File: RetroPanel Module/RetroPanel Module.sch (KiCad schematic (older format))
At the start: 58 parts, among them J1 Front Panel, J10 SW_EXTRA, J16 SPEAKER, J17 LED_HDD, J2 SW_POWER, J3 LED_POWER, J4 SW_RESET, J5 SW_TURBO, J6 LED_TURBO, J7 POWER, J8 IIC, J9 POST_CARD, M1 Mounting_Pin, M10 Mounting_Pad, M11 Mounting_Pad, M12 Mounting_Pad, M13 Mounting_Pad, M14 Mounting_Pad, M15 Mounting_Pad, M16 Mounting_Pin, M2 Mounting_Pin, M3 Mounting_Pin, M4 Mounting_Pad, M5 Mounting_Pad, M6 Mounting_Pad, M7 Mounting_Pad, M8 Mounting_Pad, M9 Mounting_Pad, Q1 2N3904, Q2 2N3904, Q3 2N3904, Q4 2N3904

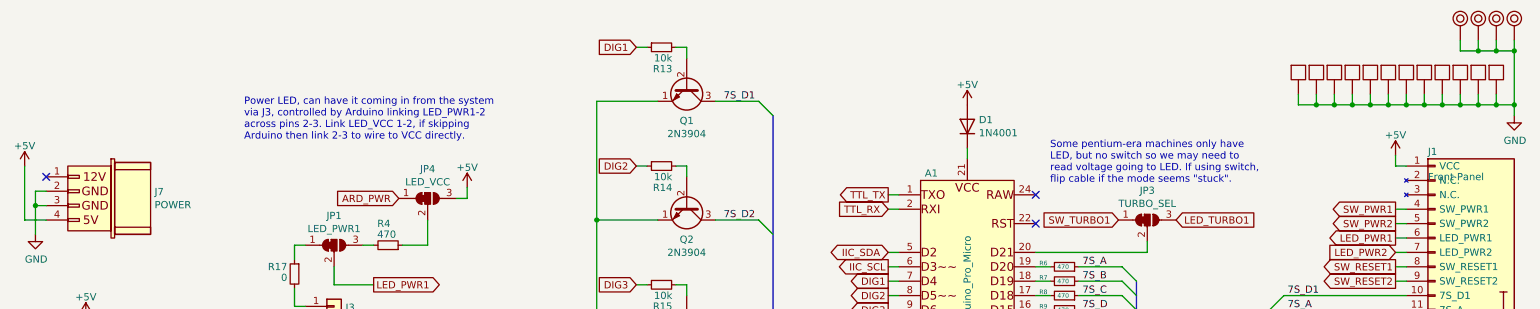
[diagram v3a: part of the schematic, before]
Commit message: Moved power diode
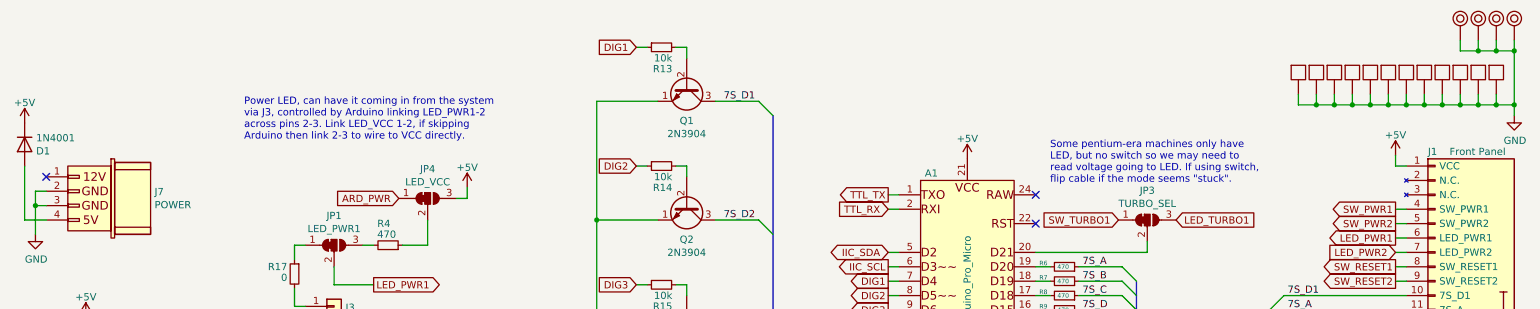
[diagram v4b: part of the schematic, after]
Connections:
- net +5V: now also A1.21 (VCC), D1.1 (K); no longer D1.2 (A), J7.4 (Pin_4)
- new net: D1.2 (A), J7.4 (Pin_4)
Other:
- moved on the sheet: D1
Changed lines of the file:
@@
 P 10525 2850
 F 0 "J1" H 10475 4150 50  0000 L CNN
-F 1 "Front Panel" H 10475 3975 50  0000 L CNN
+F 1 "Front Panel" H 10625 4150 50  0000 L CNN
 F 2 "RetroPanel:Module_Panel" H 10525 2850 50  0001 C CNN
 F 3 "~" H 10525 2850 50  0001 C CNN
@@
 $EndComp
 $Comp
-L Diode:1N4001 D1
-U 1 1 635B47F3
-P 7275 1375
-F 0 "D1" V 7321 1295 50  0000 R CNN
-F 1 "1N4001" V 7230 1295 50  0000 R CNN
-F 2 "Diode_THT:D_DO-41_SOD81_P10.16mm_Horizontal" H 7275 1200 50  0001 C CNN
-F 3 "http://www.vishay.com/docs/88503/1n4001.pdf" H 7275 1375 50  0001 C CNN
-	1    7275 1375
-	0    -1   -1   0
-$EndComp
-$Comp
 L Connector_Generic:Conn_01x02 J4
 U 1 1 635BC0CC
@@
 L power:+5V #PWR0102
 U 1 1 6370FE93
-P 7275 1225
-F 0 "#PWR0102" H 7275 1075 50  0001 C CNN
-F 1 "+5V" H 7275 1365 50  0000 C CNN
-F 2 "" H 7275 1225 50  0000 C CNN
-F 3 "" H 7275 1225 50  0000 C CNN
-	1    7275 1225
+P 7275 1600
+F 0 "#PWR0102" H 7275 1450 50  0001 C CNN
+F 1 "+5V" H 7275 1740 50  0000 C CNN
+F 2 "" H 7275 1600 50  0000 C CNN
+F 3 "" H 7275 1600 50  0000 C CNN
+	1    7275 1600
 	1    0    0    -1
 $EndComp
@@
 L power:+5V #PWR0106
 U 1 1 6371FCA6
-P 725 1650
-F 0 "#PWR0106" H 725 1500 50  0001 C CNN
-F 1 "+5V" H 725 1790 50  0000 C CNN
-F 2 "" H 725 1650 50  0000 C CNN
-F 3 "" H 725 1650 50  0000 C CNN
-	1    725  1650
+P 725 1350
+F 0 "#PWR0106" H 725 1200 50  0001 C CNN
+F 1 "+5V" H 725 1490 50  0000 C CNN
+F 2 "" H 725 1350 50  0000 C CNN
+F 3 "" H 725 1350 50  0000 C CNN
+	1    725  1350
 	1    0    0    -1
 $EndComp
@@
 Connection ~ 7950 4200
 Connection ~ 9375 3850
-Wire Wire Line
-	7275 1525 7275 1600
 Text GLabel 8325 2025 0    50   Input ~ 0
 SW_TURBO1
@@
 Wire Wire Line
 	10250 3850 10325 3850
+$Comp
+L Diode:1N4001 D1
+U 1 1 635B47F3
+P 725 1500
+F 0 "D1" V 771 1420 50  0000 R CNN
+F 1 "1N4001" V 680 1420 50  0000 R CNN
+F 2 "Diode_THT:D_DO-41_SOD81_P10.16mm_Horizontal" H 725 1325 50  0001 C CNN
+F 3 "http://www.vishay.com/docs/88503/1n4001.pdf" H 725 1500 50  0001 C CNN
+	1    725  1500
+	0    -1   1    0
+$EndComp
+Wire Bus Line
+	7950 4200 7950 4700
 Wire Bus Line
 	5925 1300 5925 3850
 Wire Bus Line
-	7950 4200 7950 4700
-Wire Bus Line
 	8450 2450 8450 3850

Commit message: Better description for CA display usage
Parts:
- Q1, Q2, Q3, Q4: value 2N3904 -> 2N3904/2N3906
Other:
- note added: "7S_TYPE Determines if 7 segment display to be\ninstalled is CA or CK - link 1-2 when used with CK\ndisplay.\n\nWhen using CA-display, link pins 2-3 as well as \nreplacing 2N3904 with 2N3906 instead. Note that\ndisplay needs to be CA variant when building it\nfor use with POST diagnostic card instead of Arduino."
- note removed: "Determines if 7 segment display is CA or\nCK - link 1-2 for CK display. When using\nCA-display, install Q1-Q4 backwards."
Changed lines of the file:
@@
 P 5325 1100
 F 0 "Q1" V 5560 1100 50  0000 C CNN
-F 1 "2N3904" V 5651 1100 50  0000 C CNN
+F 1 "2N3904/2N3906" V 5651 1100 50  0000 C CNN
 F 2 "Package_TO_SOT_THT:TO-92_Inline_Wide" H 5525 1025 50  0001 L CIN
 F 3 "https://www.onsemi.com/pub/Collateral/2N3903-D.PDF" H 5325 1100 50  0001 L CNN
@@
 P 5325 1925
 F 0 "Q2" V 5560 1925 50  0000 C CNN
-F 1 "2N3904" V 5651 1925 50  0000 C CNN
+F 1 "2N3904/2N3906" V 5651 1925 50  0000 C CNN
 F 2 "Package_TO_SOT_THT:TO-92_Inline_Wide" H 5525 1850 50  0001 L CIN
 F 3 "https://www.onsemi.com/pub/Collateral/2N3903-D.PDF" H 5325 1925 50  0001 L CNN
@@
 P 5325 2750
 F 0 "Q3" V 5560 2750 50  0000 C CNN
-F 1 "2N3904" V 5651 2750 50  0000 C CNN
+F 1 "2N3904/2N3906" V 5651 2750 50  0000 C CNN
 F 2 "Package_TO_SOT_THT:TO-92_Inline_Wide" H 5525 2675 50  0001 L CIN
 F 3 "https://www.onsemi.com/pub/Collateral/2N3903-D.PDF" H 5325 2750 50  0001 L CNN
@@
 P 5325 3575
 F 0 "Q4" V 5560 3575 50  0000 C CNN
-F 1 "2N3904" V 5651 3575 50  0000 C CNN
+F 1 "2N3904/2N3906" V 5651 3575 50  0000 C CNN
 F 2 "Package_TO_SOT_THT:TO-92_Inline_Wide" H 5525 3500 50  0001 L CIN
 F 3 "https://www.onsemi.com/pub/Collateral/2N3903-D.PDF" H 5325 3575 50  0001 L CNN
@@
 Wire Wire Line
 	4425 3900 4425 3975
-Text Notes 4200 4525 0    50   ~ 0
-Determines if 7 segment display is CA or\nCK - link 1-2 for CK display. When using\nCA-display, install Q1-Q4 backwards.
+Text Notes 4225 4950 0    50   ~ 0
+7S_TYPE Determines if 7 segment display to be\ninstalled is CA or CK - link 1-2 when used with CK\ndisplay.\n\nWhen using CA-display, link pins 2-3 as well as \nreplacing 2N3904 with 2N3906 instead. Note that\ndisplay needs to be CA variant when building it\nfor use with POST diagnostic card instead of Arduino.
 $Comp
 L Device:Speaker LS1

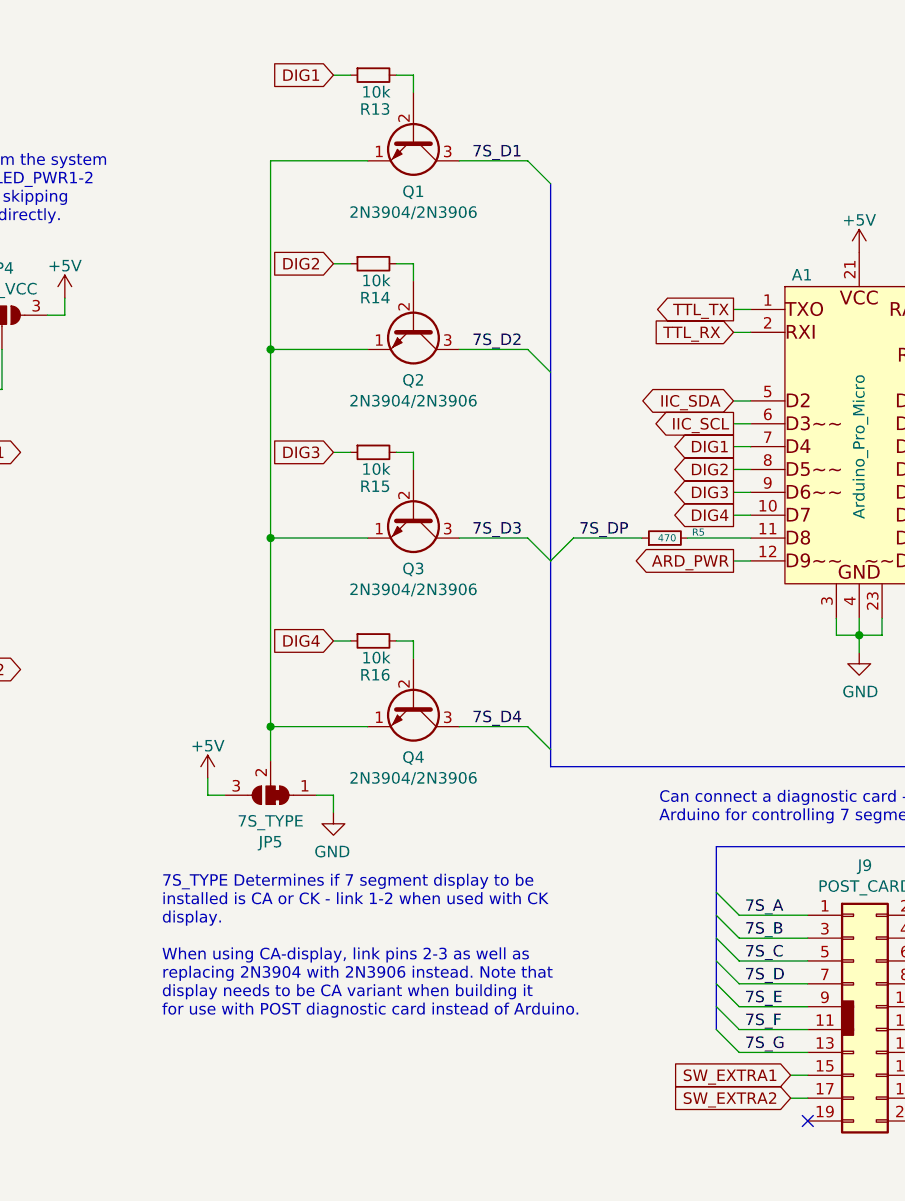
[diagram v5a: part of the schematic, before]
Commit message: Tweaked resistor value to work better 7S CA
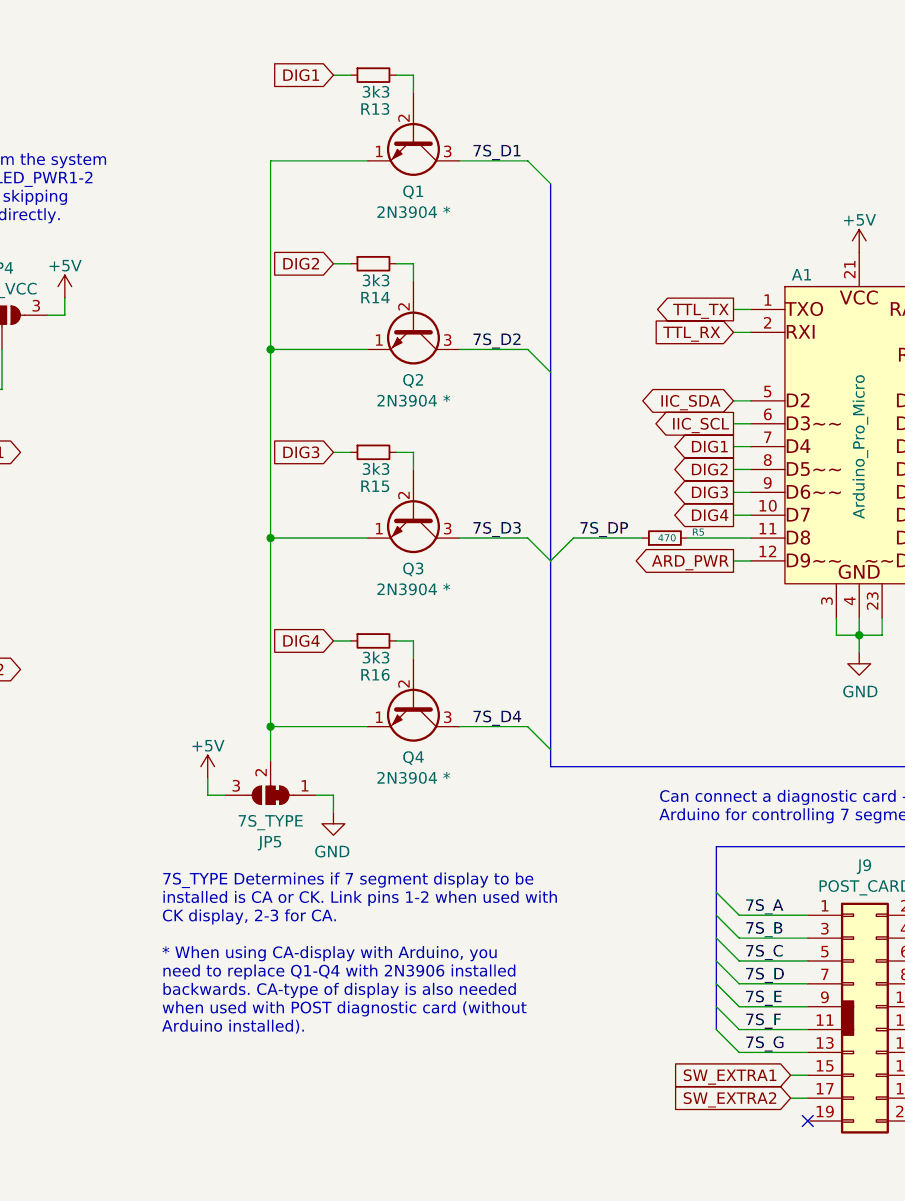
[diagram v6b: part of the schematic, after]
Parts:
- Q1, Q2, Q3, Q4: value 2N3904/2N3906 -> 2N3904 *
- R13, R14, R15, R16: value 10k -> 3k3
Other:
- note added: "7S_TYPE Determines if 7 segment display to be\ninstalled is CA or CK. Link pins 1-2 when used with\nCK display, 2-3 for CA.\n\n* When using CA-display with Arduino, you\nneed to replace Q1-Q4 with 2N3906 installed\nbackwards. CA-type of display is also needed\nwhen used with POST diagnostic card (without\nArduino installed)."
- note removed: "7S_TYPE Determines if 7 segment display to be\ninstalled is CA or CK - link 1-2 when used with CK\ndisplay.\n\nWhen using CA-display, link pins 2-3 as well as \nreplacing 2N3904 with 2N3906 instead. Note that\ndisplay needs to be CA variant when building it\nfor use with POST diagnostic card instead of Arduino."
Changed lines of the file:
@@
 P 5325 1100
 F 0 "Q1" V 5560 1100 50  0000 C CNN
-F 1 "2N3904/2N3906" V 5651 1100 50  0000 C CNN
+F 1 "2N3904 *" V 5651 1100 50  0000 C CNN
 F 2 "Package_TO_SOT_THT:TO-92_Inline_Wide" H 5525 1025 50  0001 L CIN
 F 3 "https://www.onsemi.com/pub/Collateral/2N3903-D.PDF" H 5325 1100 50  0001 L CNN
@@
 P 5150 825
 F 0 "R13" V 5300 750 50  0000 L CNN
-F 1 "10k" V 5225 750 50  0000 L CNN
+F 1 "3k3" V 5225 750 50  0000 L CNN
 F 2 "resistor:R_Axial_DIN0207_L6.3mm_D2.5mm_P10.16mm_Horizontal" H 5150 825 50  0001 C CNN
 F 3 "~" H 5150 825 50  0001 C CNN
 	1    5150 825
 	0    -1   1    0
-$EndComp
-$Comp
-L Transistor_BJT:2N3904 Q2
-U 1 1 6409DF7D
-P 5325 1925
-F 0 "Q2" V 5560 1925 50  0000 C CNN
-F 1 "2N3904/2N3906" V 5651 1925 50  0000 C CNN
-F 2 "Package_TO_SOT_THT:TO-92_Inline_Wide" H 5525 1850 50  0001 L CIN
-F 3 "https://www.onsemi.com/pub/Collateral/2N3903-D.PDF" H 5325 1925 50  0001 L CNN
-	1    5325 1925
-	0    1    1    0
 $EndComp
 Text Label 5800 2025 2    50   ~ 0
@@
 P 5150 1650
 F 0 "R14" V 5300 1575 50  0000 L CNN
-F 1 "10k" V 5225 1575 50  0000 L CNN
+F 1 "3k3" V 5225 1575 50  0000 L CNN
 F 2 "resistor:R_Axial_DIN0207_L6.3mm_D2.5mm_P10.16mm_Horizontal" H 5150 1650 50  0001 C CNN
 F 3 "~" H 5150 1650 50  0001 C CNN
@@
 P 5325 2750
 F 0 "Q3" V 5560 2750 50  0000 C CNN
-F 1 "2N3904/2N3906" V 5651 2750 50  0000 C CNN
+F 1 "2N3904 *" V 5651 2750 50  0000 C CNN
 F 2 "Package_TO_SOT_THT:TO-92_Inline_Wide" H 5525 2675 50  0001 L CIN
 F 3 "https://www.onsemi.com/pub/Collateral/2N3903-D.PDF" H 5325 2750 50  0001 L CNN
@@
 P 5150 2475
 F 0 "R15" V 5300 2400 50  0000 L CNN
-F 1 "10k" V 5225 2400 50  0000 L CNN
+F 1 "3k3" V 5225 2400 50  0000 L CNN
 F 2 "resistor:R_Axial_DIN0207_L6.3mm_D2.5mm_P10.16mm_Horizontal" H 5150 2475 50  0001 C CNN
 F 3 "~" H 5150 2475 50  0001 C CNN
@@
 P 5325 3575
 F 0 "Q4" V 5560 3575 50  0000 C CNN
-F 1 "2N3904/2N3906" V 5651 3575 50  0000 C CNN
+F 1 "2N3904 *" V 5651 3575 50  0000 C CNN
 F 2 "Package_TO_SOT_THT:TO-92_Inline_Wide" H 5525 3500 50  0001 L CIN
 F 3 "https://www.onsemi.com/pub/Collateral/2N3903-D.PDF" H 5325 3575 50  0001 L CNN
@@
 P 5150 3300
 F 0 "R16" V 5300 3225 50  0000 L CNN
-F 1 "10k" V 5225 3225 50  0000 L CNN
+F 1 "3k3" V 5225 3225 50  0000 L CNN
 F 2 "resistor:R_Axial_DIN0207_L6.3mm_D2.5mm_P10.16mm_Horizontal" H 5150 3300 50  0001 C CNN
 F 3 "~" H 5150 3300 50  0001 C CNN
@@
 Wire Wire Line
 	4425 3900 4425 3975
-Text Notes 4225 4950 0    50   ~ 0
-7S_TYPE Determines if 7 segment display to be\ninstalled is CA or CK - link 1-2 when used with CK\ndisplay.\n\nWhen using CA-display, link pins 2-3 as well as \nreplacing 2N3904 with 2N3906 instead. Note that\ndisplay needs to be CA variant when building it\nfor use with POST diagnostic card instead of Arduino.
+Text Notes 4225 5025 0    50   ~ 0
+7S_TYPE Determines if 7 segment display to be\ninstalled is CA or CK. Link pins 1-2 when used with\nCK display, 2-3 for CA.\n\n* When using CA-display with Arduino, you\nneed to replace Q1-Q4 with 2N3906 installed\nbackwards. CA-type of display is also needed\nwhen used with POST diagnostic card (without\nArduino installed).
 $Comp
 L Device:Speaker LS1
@@
 Wire Bus Line
 	9375 2650 9375 3850
+$Comp
+L Transistor_BJT:2N3904 Q2
+U 1 1 6409DF7D
+P 5325 1925
+F 0 "Q2" V 5560 1925 50  0000 C CNN
+F 1 "2N3904 *" V 5651 1925 50  0000 C CNN
+F 2 "Package_TO_SOT_THT:TO-92_Inline_Wide" H 5525 1850 50  0001 L CIN
+F 3 "https://www.onsemi.com/pub/Collateral/2N3903-D.PDF" H 5325 1925 50  0001 L CNN
+	1    5325 1925
+	0    1    1    0
+$EndComp
 $EndSCHEMATC
